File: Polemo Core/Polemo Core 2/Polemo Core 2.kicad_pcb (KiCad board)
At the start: 4 copper layers, 40 x 100 mm, 174 parts, among them P1 Header-Male-2.54_2x2, P2 Header-Male-2.54_2x2, Q1 BC847_C2910145, Q2 MMBT5551LT1G, Q3 AO3401A, Q4 AO3401A, Q5 MMBT5551LT1G, U1 ATSAML21G18B-AUT, U10 74LVC1G08GV,125, U11 LT3014BHVES5#TRMPBF, U12 TXU0202DCUR, U13 TLV7031DBVR, U14 TLR341G-GTR, U15 803-87-006-10-001101, U2 XC6209F332MR-G, U3 MC14043BDR2G, U4 LMV793MFX/NOPB, U5 TPS7A2030PDBVR, U6 TLV3201AIDBVT, U7 OPA357AIDBVR, U8 TLR341G-GTR, U9 MF-ASML020/6-2, X1 32.768kHz

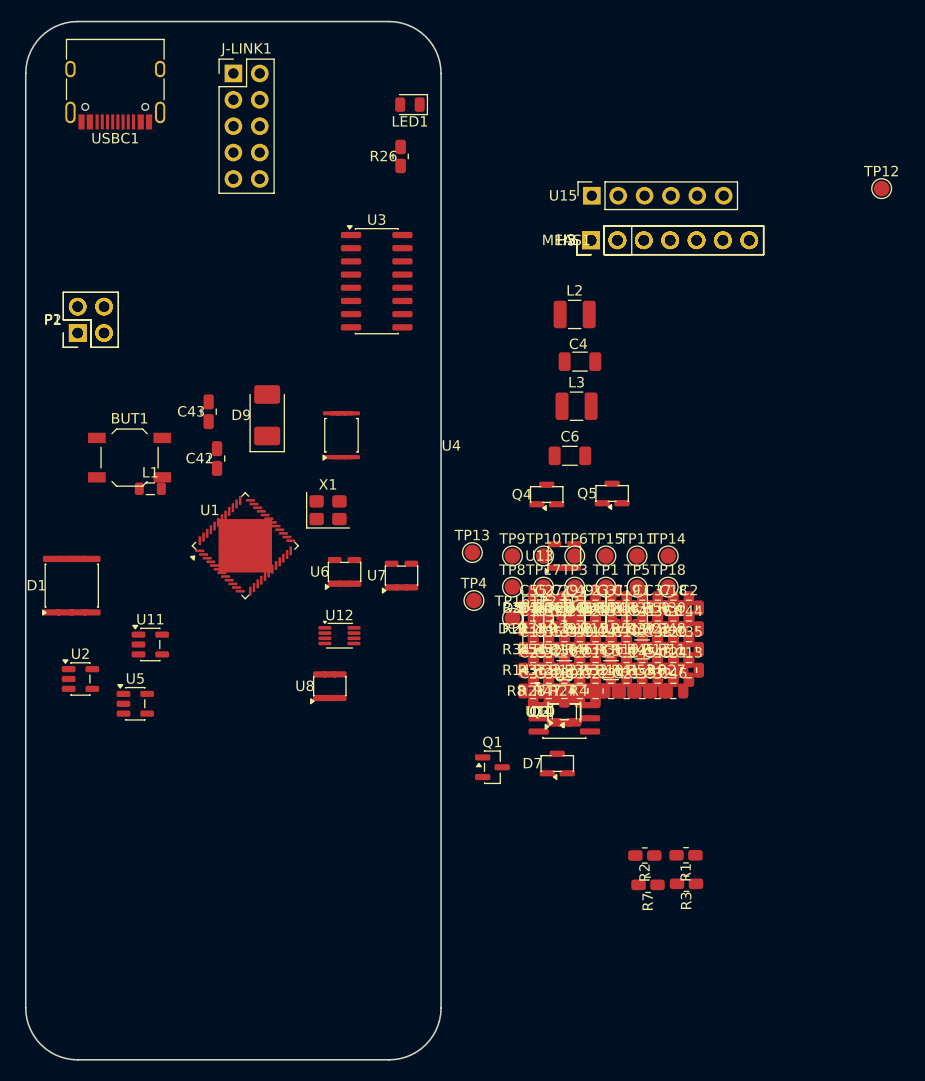
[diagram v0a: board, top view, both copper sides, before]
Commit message: Add scripts for backside and frontside silkscreen text, and refine component placement
- Implemented `add_backside_text.py` to add silkscreen text to the backside of the PomeloCore PCB based on a reference image.
- Implemented `add_frontside_text.py` to add silkscreen text to the front side of the PomeloCore PCB, including branding and component labels.
- Created `refine_placement.py` to update component positions based on a detailed top-side reference image, improving layout organization and alignment.
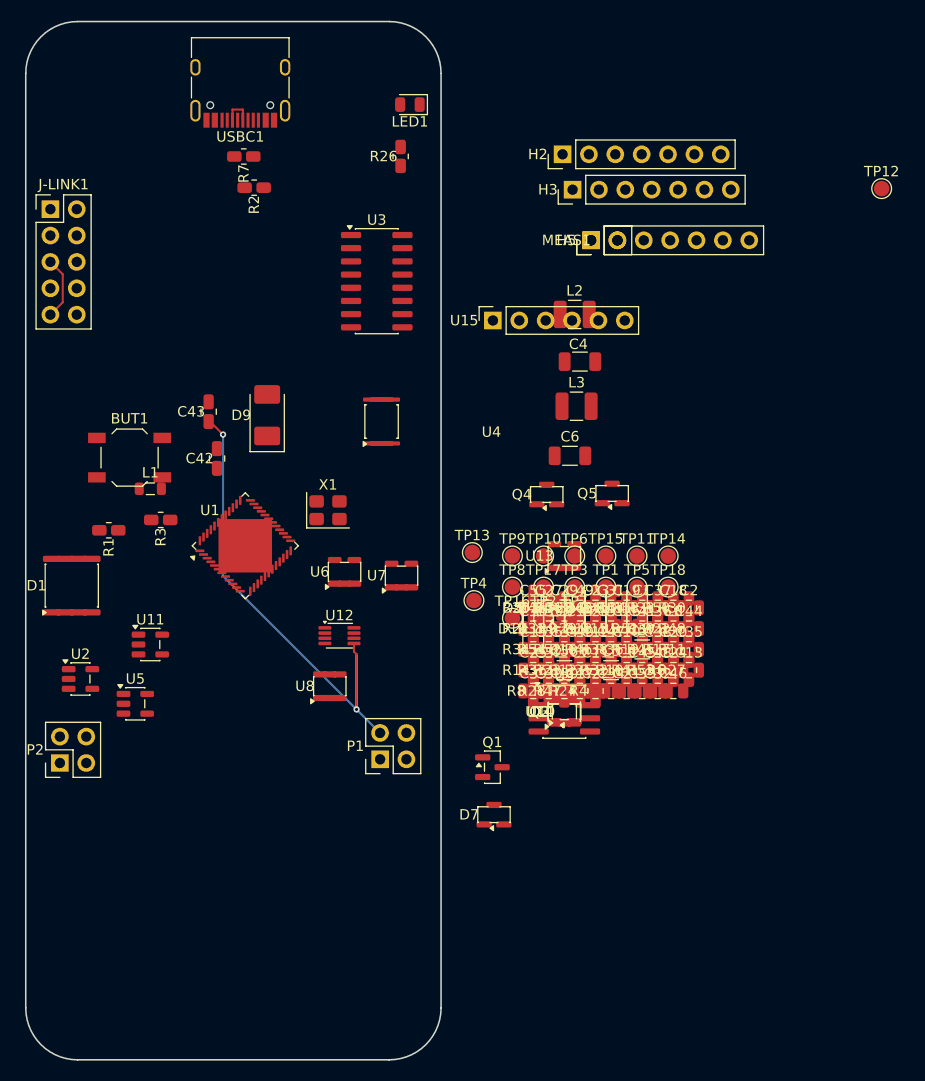
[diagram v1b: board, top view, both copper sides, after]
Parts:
- moved R7 80.2 mm to (71.0, 63.0)
- moved R2 74.5 mm to (72.0, 66.0)
- moved R1 63.8 mm to (58.0, 99.0)
- moved R3 61.6 mm to (63.0, 98.0)
- moved P1 50.3 mm to (84.1, 121.1)
- moved P2 41.4 mm to (53.3, 121.4)
- moved J-LINK1 21.9 mm to (52.4, 68.1)
- moved U15 15.3 mm to (95.0, 78.8)
- moved USBC1 12.0 mm to (70.7, 55.5)
- moved H2 8.72 mm to (101.7, 62.8)
- moved D7 7.84 mm to (95.1, 126.4)
- moved H3 5.19 mm to (102.7, 66.2)
- moved U4 4.08 mm to (84.3, 88.5)
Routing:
- net GND: track 0.00 -> 60.6 mm, vias 0 -> 2
- net USBDP: track 0.00 -> 3.05 mm
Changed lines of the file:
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@@
 	(footprint "Connector_PinHeader_2.54mm:PinHeader_1x07_P2.54mm_Vertical"
 		(layer "F.Cu")
-		(at 104.4448 71.0692 90)
+		(at 101.7016 62.7888 90)
 		(descr "Through hole straight pin header, 1x07, 2.54mm pitch, single row")
 		(tags "Through hole pin header THT 1x07 2.54mm single row")
@@
 	(footprint "Connector_PinHeader_2.54mm:PinHeader_2x02_P2.54mm_Vertical"
 		(layer "F.Cu")
-		(at 55 80 90)
+		(at 84.1248 121.0564 90)
 		(descr "Through hole straight pin header, 2x02, 2.54mm pitch, double rows")
 		(tags "Through hole pin header THT 2x02 2.54mm double row")
@@
 	(footprint "Connector_PinHeader_2.54mm:PinHeader_2x05_P2.54mm_Vertical"
 		(layer "F.Cu")
-		(at 70 55)
+		(at 52.3748 68.072)
 		(descr "Through hole straight pin header, 2x05, 2.54mm pitch, double rows")
 		(tags "Through hole pin header THT 2x05 2.54mm double row")
@@
 	(footprint "Connector_PinHeader_2.54mm:PinHeader_1x07_P2.54mm_Vertical"
 		(layer "F.Cu")
-		(at 104.4448 71.0692 90)
+		(at 102.6668 66.1924 90)
 		(descr "Through hole straight pin header, 1x07, 2.54mm pitch, single row")
 		(tags "Through hole pin header THT 1x07 2.54mm single row")
@@
 	(footprint "Connector_PinSocket_2.54mm:PinSocket_1x06_P2.54mm_Vertical"
 		(layer "F.Cu")
-		(at 104.5206 66.777 90)
+		(at 94.996 78.7908 90)
 		(descr "Through hole straight socket strip, 1x06, 2.54mm pitch, single row (from Kicad 4.0.7), script generated")
 		(tags "Through hole socket strip THT 1x06 2.54mm single row")
@@
 	(footprint "Connector_PinHeader_2.54mm:PinHeader_2x02_P2.54mm_Vertical"
 		(layer "F.Cu")
-		(at 55 80 90)
+		(at 53.2892 121.412 90)
 		(descr "Through hole straight pin header, 2x02, 2.54mm pitch, double rows")
 		(tags "Through hole pin header THT 2x02 2.54mm double row")
@@
 	(footprint "Package_SO:MSOP-8_3x3mm_P0.65mm"
 		(layer "F.Cu")
-		(at 80.4066 89.8441 90)
+		(at 84.2674 88.5233 90)
 		(descr "MSOP, 8 Pin (https://www.jedec.org/system/files/docs/mo-187F.pdf variant AA), generated with kicad-footprint-generator ipc_gullwing_generator.py")
 		(tags "MSOP SO")
@@
 	)
 	(footprint "Resistor_SMD:R_0805_2012Metric"
+		(placed yes)
 		(layer "F.Cu")
-		(at 113.5907 130.302 180)
+		(at 58 99 180)
 		(descr "Resistor SMD 0805 (2012 Metric), square (rectangular) end terminal, IPC-7351 nominal, (Body size source: IPC-SM-782 page 72, https://www.pcb-3d.com/wordpress/wp-content/uploads/ipc-sm-782a_amendment_1_and_2.pdf), generated with kicad-footprint-generator")
 		(tags "resistor")
@@
 	(footprint "Connector_USB:USB_C_Receptacle_HRO_TYPE-C-31-M-12"
 		(layer "F.Cu")
-		(at 58.6232 55.6248 180)
+		(at 70.6608 55.4568 180)
 		(descr "USB Type-C receptacle for USB 2.0 and PD, http://www.krhro.com/uploads/soft/180320/1-1P320120243.pdf")
 		(tags "usb usb-c 2.0 pd")
@@
 	(footprint "Package_DFN_QFN:QFN-48-1EP_7x7mm_P0.5mm_EP5.15x5.15mm"
 		(layer "F.Cu")
-		(at 71.143911 100.49087 45)
+		(at 71.1439 100.4909 45)
 		(descr "QFN, 48 Pin (http://www.analog.com/media/en/package-pcb-resources/package/pkg_pdf/ltc-legacy-qfn/QFN_48_05-08-1704.pdf), generated with kicad-footprint-generator ipc_noLead_generator.py")
 		(tags "QFN NoLead")
@@
 	)
 	(footprint "Resistor_SMD:R_0805_2012Metric"
+		(placed yes)
 		(layer "F.Cu")
-		(at 109.9331 133.1468 180)
+		(at 71 63 180)
 		(descr "Resistor SMD 0805 (2012 Metric), square (rectangular) end terminal, IPC-7351 nominal, (Body size source: IPC-SM-782 page 72, https://www.pcb-3d.com/wordpress/wp-content/uploads/ipc-sm-782a_amendment_1_and_2.pdf), generated with kicad-footprint-generator")
 		(tags "resistor")
@@
 	)
 	(footprint "Resistor_SMD:R_0805_2012Metric"
+		(placed yes)
 		(layer "F.Cu")
-		(at 113.6396 133.0452 180)
+		(at 63 98 180)
 		(descr "Resistor SMD 0805 (2012 Metric), square (rectangular) end terminal, IPC-7351 nominal, (Body size source: IPC-SM-782 page 72, https://www.pcb-3d.com/wordpress/wp-content/uploads/ipc-sm-782a_amendment_1_and_2.pdf), generated with kicad-footprint-generator")
 		(tags "resistor")
@@
 	)
 	(footprint "Resistor_SMD:R_0805_2012Metric"
+		(placed yes)
 		(layer "F.Cu")
-		(at 109.627 130.3214 180)
+		(at 72 66 180)
 		(descr "Resistor SMD 0805 (2012 Metric), square (rectangular) end terminal, IPC-7351 nominal, (Body size source: IPC-SM-782 page 72, https://www.pcb-3d.com/wordpress/wp-content/uploads/ipc-sm-782a_amendment_1_and_2.pdf), generated with kicad-footprint-generator")
 		(tags "resistor")
@@
 	(footprint "Package_TO_SOT_SMD:SOT-23"
 		(layer "F.Cu")
-		(at 101.1936 121.4628 90)
+		(at 95.0976 126.3904 90)
 		(descr "SOT, 3 Pin (JEDEC TO-236 Var AB https://www.jedec.org/document_search?search_api_views_fulltext=TO-236), generated with kicad-footprint-generator ipc_gullwing_generator.py")
 		(tags "SOT TO_SOT_SMD")
@@
 		)
 	)
+	(segment
+		(start 67.6148 88.5292)
+		(end 67.7552 88.5292)
+		(width 0.2)
+		(layer "F.Cu")
+		(net 1)
+	)
+	(segment
+		(start 69.003 89.9009)
+		(end 69.003 89.777)
+		(width 0.2)
+		(layer "F.Cu")
+		(net 1)
+	)
+	(segment
+		(start 69.003 89.777)
+		(end 69.003 89.9009)
+		(width 0.2)
+		(layer "F.Cu")
+		(net 1)
+	)
+	(segment
+		(start 53.5654 77.0414)
+		(end 53.5654 74.3426)
+		(width 0.2)
+		(layer "F.Cu")
+		(net 1)
+	)
+	(segment
+		(start 52.3748 78.232)
+		(end 53.5654 77.0414)
+		(width 0.2)
+		(layer "F.Cu")
+		(net 1)
+	)
+	(segment
+		(start 81.8625 110.932)
+		(end 81.8625 116.254)
+		(width 0.2)
+		(layer "F.Cu")
+		(net 1)
+	)
+	(segment
+		(start 67.7552 88.5292)
+		(end 69.003 89.777)
+		(width 0.2)
+		(layer "F.Cu")
+		(net 1)
+	)
+	(segment
+		(start 81.6132 110.682)
+		(end 81.8625 110.932)
+		(width 0.2)
+		(layer "F.Cu")
+		(net 1)
+	)
+	(segment
+		(start 53.5654 74.3426)
+		(end 52.3748 73.152)
+		(width 0.2)
+		(layer "F.Cu")
+		(net 1)
+	)
+	(segment
+		(start 81.6132 109.9)
+		(end 81.6132 110.682)
+		(width 0.2)
+		(layer "F.Cu")
+		(net 1)
+	)
+	(via
+		(at 69.003 89.777)
+		(size 0.6)
+		(drill 0.3)
+		(layers "F.Cu" "B.Cu")
+		(net 1)
+	)
+	(via
+		(at 81.8625 116.254)
+		(size 0.6)
+		(drill 0.3)
+		(layers "F.Cu" "B.Cu")
+		(net 1)
+	)
+	(segment
+		(start 83.5947 117.986)
+		(end 84.1248 118.516)
+		(width 0.2)
+		(layer "B.Cu")
+		(net 1)
+	)
+	(segment
+		(start 81.8625 110.932)
+		(end 81.8625 116.254)
+		(width 0.2)
+		(layer "B.Cu")
+		(net 1)
+	)
+	(segment
+		(start 81.8625 116.254)
+		(end 83.5946 117.986)
+		(width 0.2)
+		(layer "B.Cu")
+		(net 1)
+	)
+	(segment
+		(start 81.8625 110.932)
+		(end 81.8625 116.254)
+		(width 0.2)
+		(layer "B.Cu")
+		(net 1)
+	)
+	(segment
+		(start 83.5946 117.986)
+		(end 83.5947 117.986)
+		(width 0.2)
+		(layer "B.Cu")
+		(net 1)
+	)
+	(segment
+		(start 69.003 89.777)
+		(end 69.003 103.395)
+		(width 0.2)
+		(layer "B.Cu")
+		(net 1)
+	)
+	(segment
+		(start 69.003 89.9009)
+		(end 69.003 89.777)
+		(width 0.2)
+		(layer "B.Cu")
+		(net 1)
+	)
+	(segment
+		(start 69.003 89.777)
+		(end 69.003 89.9009)
+		(width 0.2)
+		(layer "B.Cu")
+		(net 1)
+	)
+	(segment
+		(start 69.003 103.395)
+		(end 81.8625 116.254)
+		(width 0.2)
+		(layer "B.Cu")
+		(net 1)
+	)
+	(segment
+		(start 69.9108 58.4751)
+		(end 70.9108 58.4751)
+		(width 0.2)
+		(layer "F.Cu")
+		(net 27)
+	)
+	(segment
+		(start 69.9108 59.5018)
+		(end 69.9108 58.4751)
+		(width 0.2)
+		(layer "F.Cu")
+		(net 27)
+	)
+	(segment
+		(start 70.9108 59.5018)
+		(end 70.9108 58.4751)
+		(width 0.2)
+		(layer "F.Cu")
+		(net 27)
+	)
 	(embedded_fonts no)

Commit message: Added older version
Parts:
- moved USBC1 91.0 mm to (87.0, 145.0), turned to 0 degrees
- moved R7 79.1 mm to (84.0, 141.0), turned to 0 degrees
- moved R2 77.9 mm to (84.0, 143.0), turned to 0 degrees
- moved LED1 74.0 mm to (87.0, 132.0)
- moved R26 71.0 mm to (85.0, 134.0)
- moved H3 63.8 mm to (52.0, 105.0), turned to 0 degrees
- moved U3 61.0 mm to (62.0, 132.0)
- moved C44 56.5 mm to (64.0, 82.0)
- moved R32 56.2 mm to (72.0, 68.0)
- moved C10 56.2 mm to (62.0, 78.0)
- moved R13 55.5 mm to (63.0, 72.0)
- moved C4 55.1 mm to (72.0, 128.0)
- moved H2 54.4 mm to (52.0, 85.0), turned to 0 degrees
- moved C23 54.2 mm to (70.0, 65.0)
- moved R24 53.4 mm to (71.0, 72.0)
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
